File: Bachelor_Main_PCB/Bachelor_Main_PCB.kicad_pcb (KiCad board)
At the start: 4 copper layers, 200 x 81.5 mm, 220 parts, among them IC1 LD3985M18R, J1 M20-9990245, J11 F32Q-1A7H1-11022, J13 CONMHF1-SMD-G-T, J14 CONMHF1-SMD-G-T, J2 M20-9990245, J21 CONMHF1-SMD-G-T, J25 M20-9990245, J26 691137710002, J27 Conn_01x03_Pin, J28 691137710002, J29 M20-9990245, J4 MEM2075-00-140-01-A, J8 Conn_01x07_Pin, J9 M20-9990245, P1 SF70S006VBAR2000, Q1 SSM3J358R,LF, Q10 NX3008NBKW, Q11 SSM3J358R,LF, Q12 NX3008NBKW, Q13 BC817-40Q-13-F, Q2 SSM3J358R,LF, Q3 NX3008NBKW, Q4 NX3008NBKW, Q5 NX3008NBKW, Q6 NX3008NBKW, Q7 NX3008NBKW, Q8 NX3008NBKW, Q9 NX3008NBKW, U1 USB3320C-EZK-TR, U10 LMR51450FNDRRR, U11 USB2514B-I/M2, U2 STM32H7A3ZITxQ, U3 ESD7004MUTAG, U4 ESD7004MUTAG, U5 SC0683, U6 ESD7004MUTAG, U7 RC7620_1104627, U8 LM73100RPWR, U9 LMR51450FNDRRR, Y1 ECS-327TXO-30-TR, Y2 SG-210STF 24Mhz

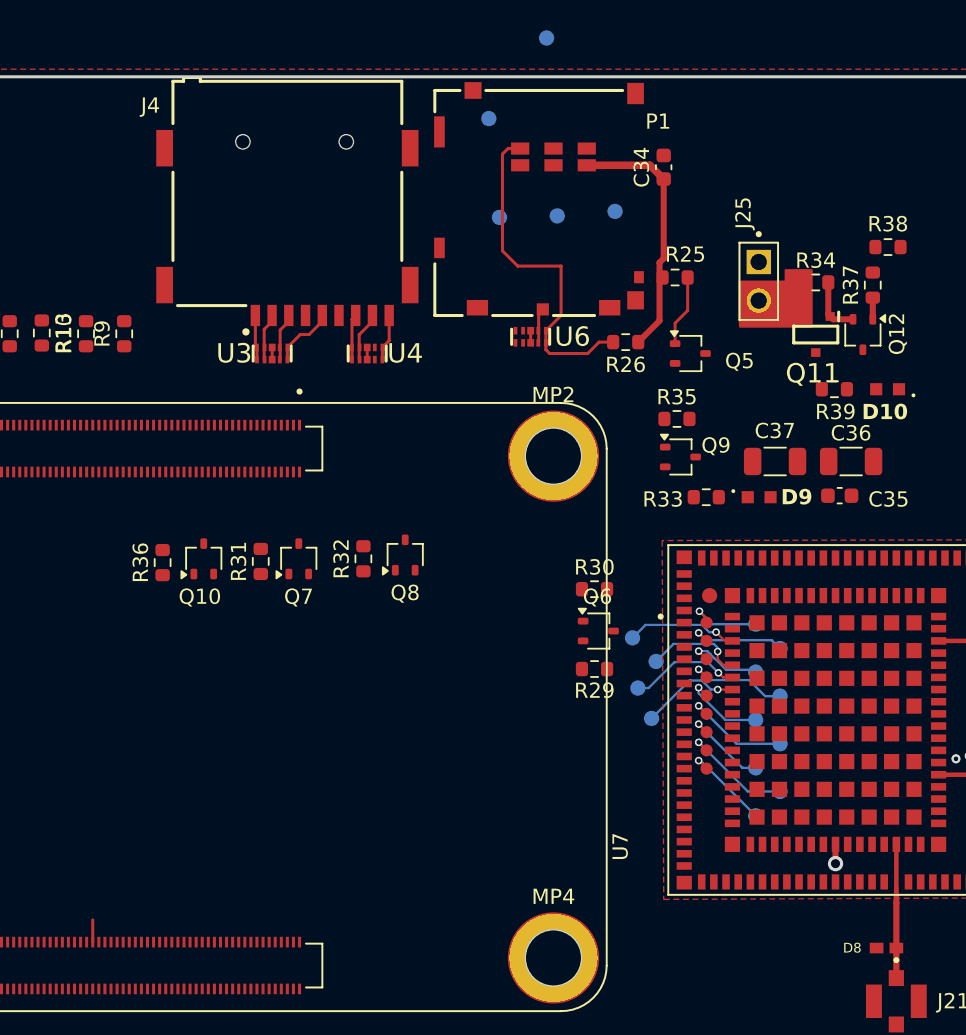
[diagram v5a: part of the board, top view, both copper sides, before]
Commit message: Route SIMcard and 3v5 modem
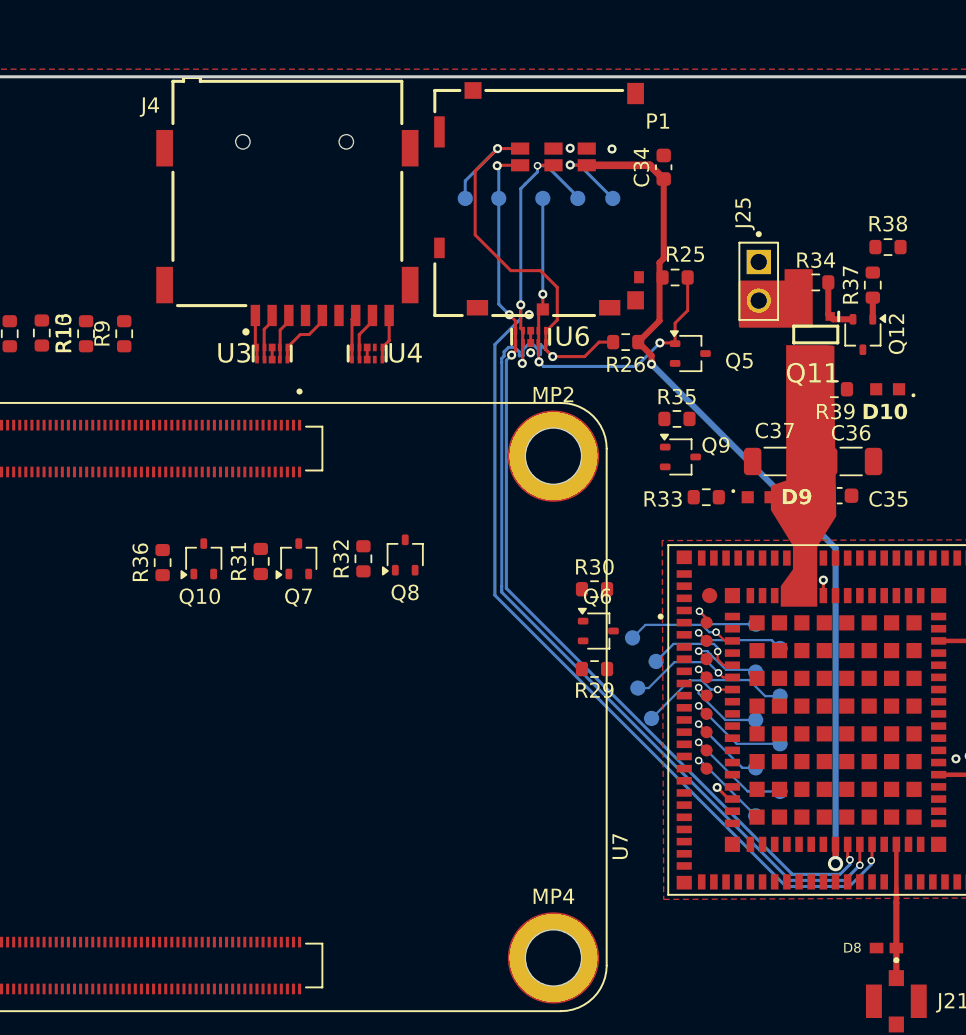
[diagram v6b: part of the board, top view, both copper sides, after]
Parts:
- moved T6 10.6 mm to (206.3, 50.5), turned to 180 degrees
- moved T7 5.47 mm to (201.2, 50.5), turned to 180 degrees
- moved T9 1.77 mm to (208.6, 50.5), turned to 180 degrees
- moved T8 1.25 mm to (203.4, 50.5), turned to 180 degrees
- moved T10 0.86 mm to (210.9, 50.5), turned to 180 degrees
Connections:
- U6 pad 4: /Wireless modem/UIM_CLK -> /Wireless modem/UIM_RESET_N
- U6 pad 5: /Wireless modem/UIM_RESET_N -> /Wireless modem/UIM_CLK
- U6 pad 6: /Wireless modem/UIM_RESET_N -> /Wireless modem/UIM_CLK
- U6 pad 7: /Wireless modem/UIM_CLK -> /Wireless modem/UIM_RESET_N
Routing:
- net /Wireless modem/UIM_RESET_N: track 0.00 -> 72.5 mm, vias 0 -> 4
- net /Wireless modem/UIM_CLK: track 0.00 -> 62.1 mm, vias 0 -> 4
- net /Wireless modem/UIM_DATA: track 22.7 -> 83.0 mm, vias 0 -> 3
- net /Wireless modem/UIM_VCC: track 18.1 -> 62.6 mm, vias 1 -> 3
- net Net-(Q5-G): track 7.29 -> 25.7 mm, vias 0 -> 3
- net unconnected-(U5B-DSI0_C_N-Pad169): track 1.46 -> 0.00 mm
- net +3V5_MODEM: track 0.00 -> 1.32 mm, vias 0 -> 1
- net /Wireless modem/1V8_TX_ON: track 0.00 -> 1.02 mm, vias 0 -> 1
- net GND: vias 26 -> 30
